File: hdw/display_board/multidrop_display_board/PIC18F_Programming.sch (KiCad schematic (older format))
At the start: 0 parts

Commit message: more sch work
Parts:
- added C801, C802: 0.1uF, Capacitors_SMD:C_0603, symbol Custom_Library:C_Custom
- added J801: PICKIT4, Custom Footprints Library:PICKIT4_Header, symbol Connector_Generic:Conn_01x08
- added Q801, Q?: BSS214NW, Package_TO_SOT_SMD:SOT-323_SC-70, symbol Transistor_FET:BSS214NW
- added R802, R804, R?: 10k, Resistors_SMD:R_0603, symbol Custom_Library:R_Custom
- added R805: 1k, Resistors_SMD:R_0603, symbol Custom_Library:R_Custom
- added SW801: MRST, Buttons_Switches_THT:SW_PUSH_6mm, symbol Switch:SW_Push
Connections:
- new net: C801.1, Q801.3 (D), Q?.3 (D), R804.2, R805.2
- new net: Q801.1 (G), R802.1, SW801.2
- new net +5V: C802.1, J801.2 (Pin_2), R804.1, SW801.1
- new net EXT_RESET: Q?.1 (G), R?.1
- new net GND: C801.2, C802.2, J801.3 (Pin_3), Q801.2 (S), Q?.2 (S), R802.2, R?.2
- new net PIC18F_ICSPCLK: J801.5 (Pin_5)
- new net PIC18F_ICSPDAT: J801.4 (Pin_4)
- new net ~PIC18F_MCLR: J801.1 (Pin_1), R805.1
- no-connect marks 0 -> 3

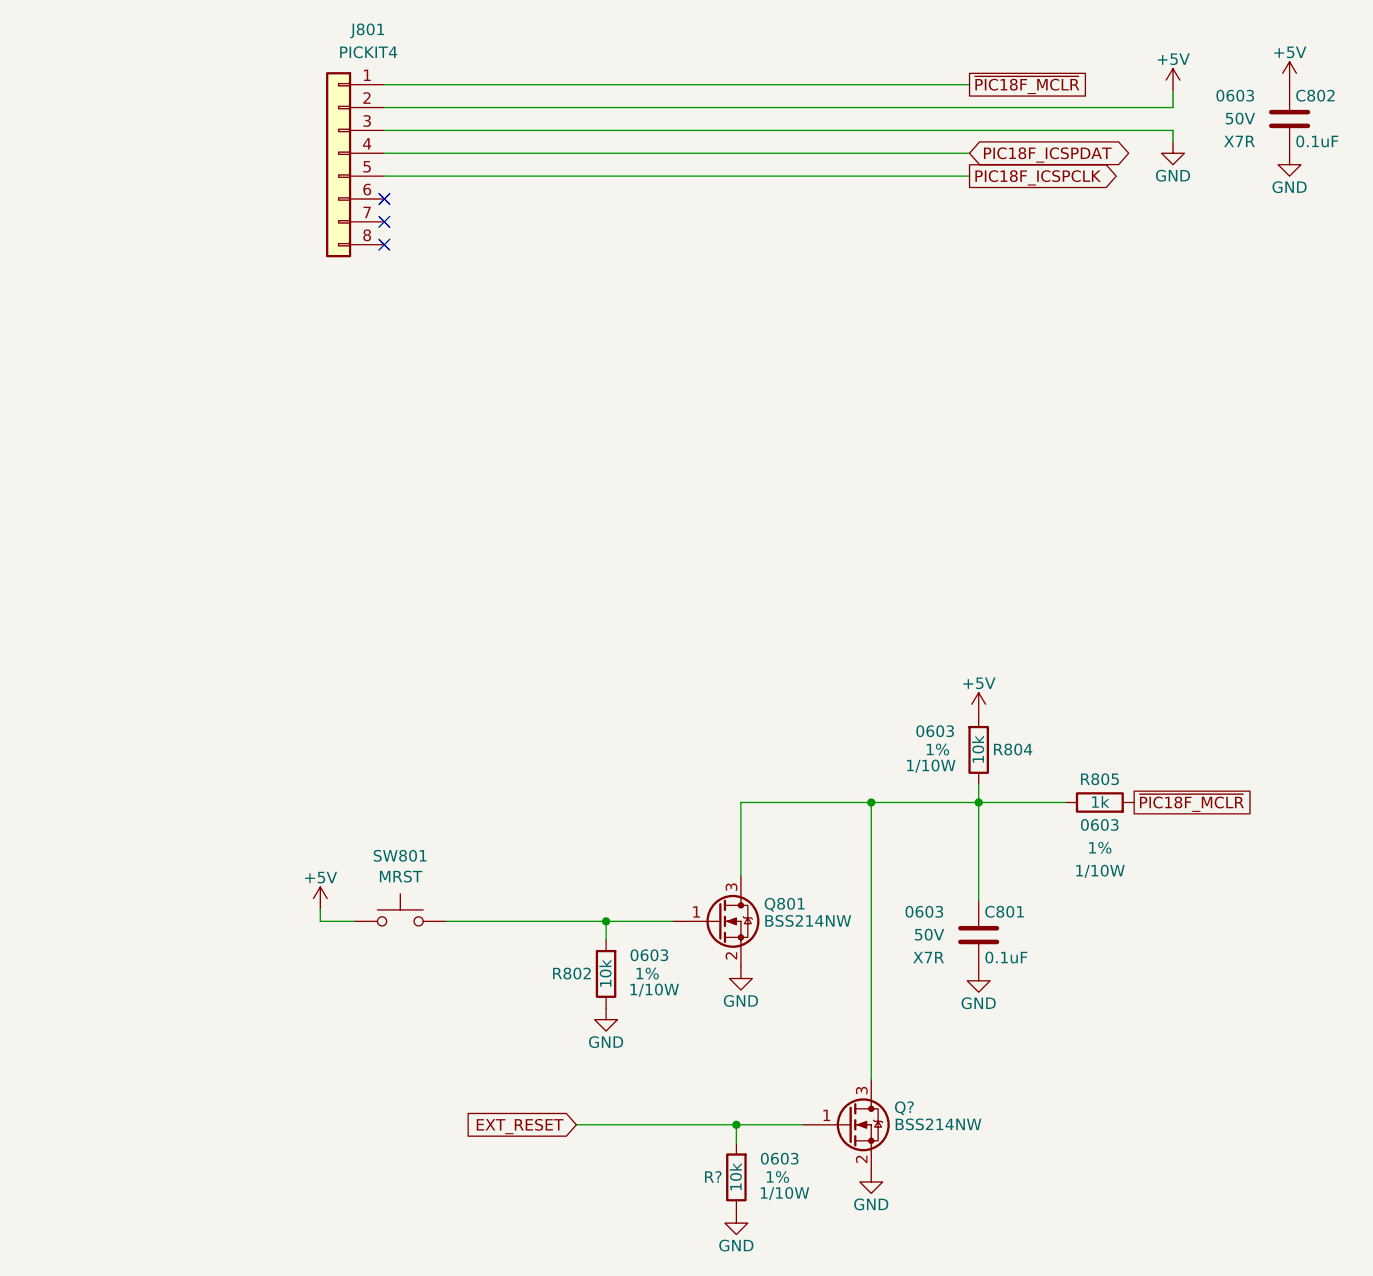
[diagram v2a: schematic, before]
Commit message: Added LED drivers, IO connectors to SCH
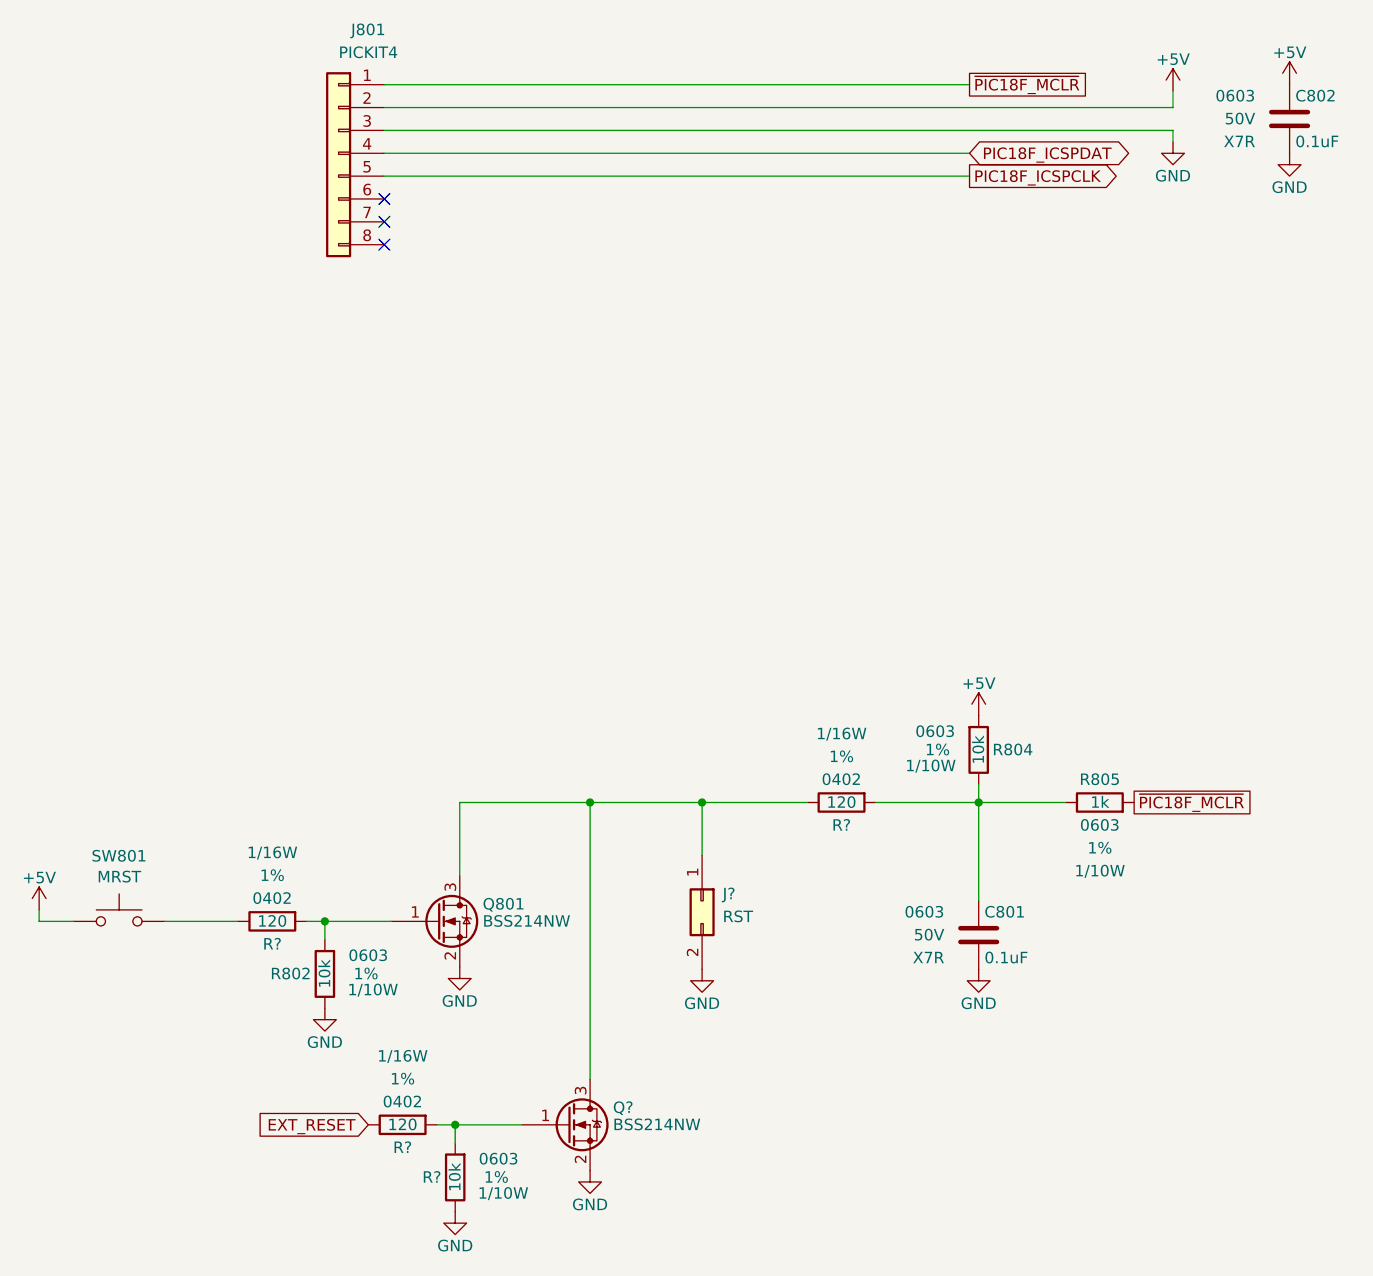
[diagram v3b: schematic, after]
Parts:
- added J?: RST, symbol Connector_Generic:Conn_02x01
- added R? (x3): 120, symbol Custom_Library:R_Custom
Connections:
- net EXT_RESET: now also R?.2; no longer Q?.1 (G), R?.1
- net GND: now also J?.2 (Pin_2)
- net at C801.1, R804.2, R805.2: now also R?.1; no longer Q801.3 (D), Q?.3 (D)
- net at Q801.1 (G), R802.1: now also R?.1; no longer SW801.2
- new net: R?.2, SW801.2
- new net: J?.1 (Pin_1), Q801.3 (D), Q?.3 (D), R?.2
- new net: Q?.1 (G), R?.1, R?.1
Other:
- moved on the sheet: Q801, Q?, R802, R?, SW801
